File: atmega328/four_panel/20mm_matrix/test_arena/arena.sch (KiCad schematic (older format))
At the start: 35 parts, among them P1 CONN15, P10 CONN_2X2, P11 CONN_2X2, P12 CONN_2X2, P13 CONN_2X2, P14 CONN_2X2, P15 CONN_2X2, P16 CONN_2X2, P17 CONN_2X2, P18 CONN_2X2, P19 CONN_2X2, P2 CONN15, P20 CONN_2X2, P21 CONN_2X2, P22 CONN_20X2, P23 CONN_30X2, P24 CONN_2, P3 CONN15, P4 CONN15, P5 CONN15, P6 CONN15, P7 CONN_2X2, P8 CONN_2X2, P9 CONN_2X2

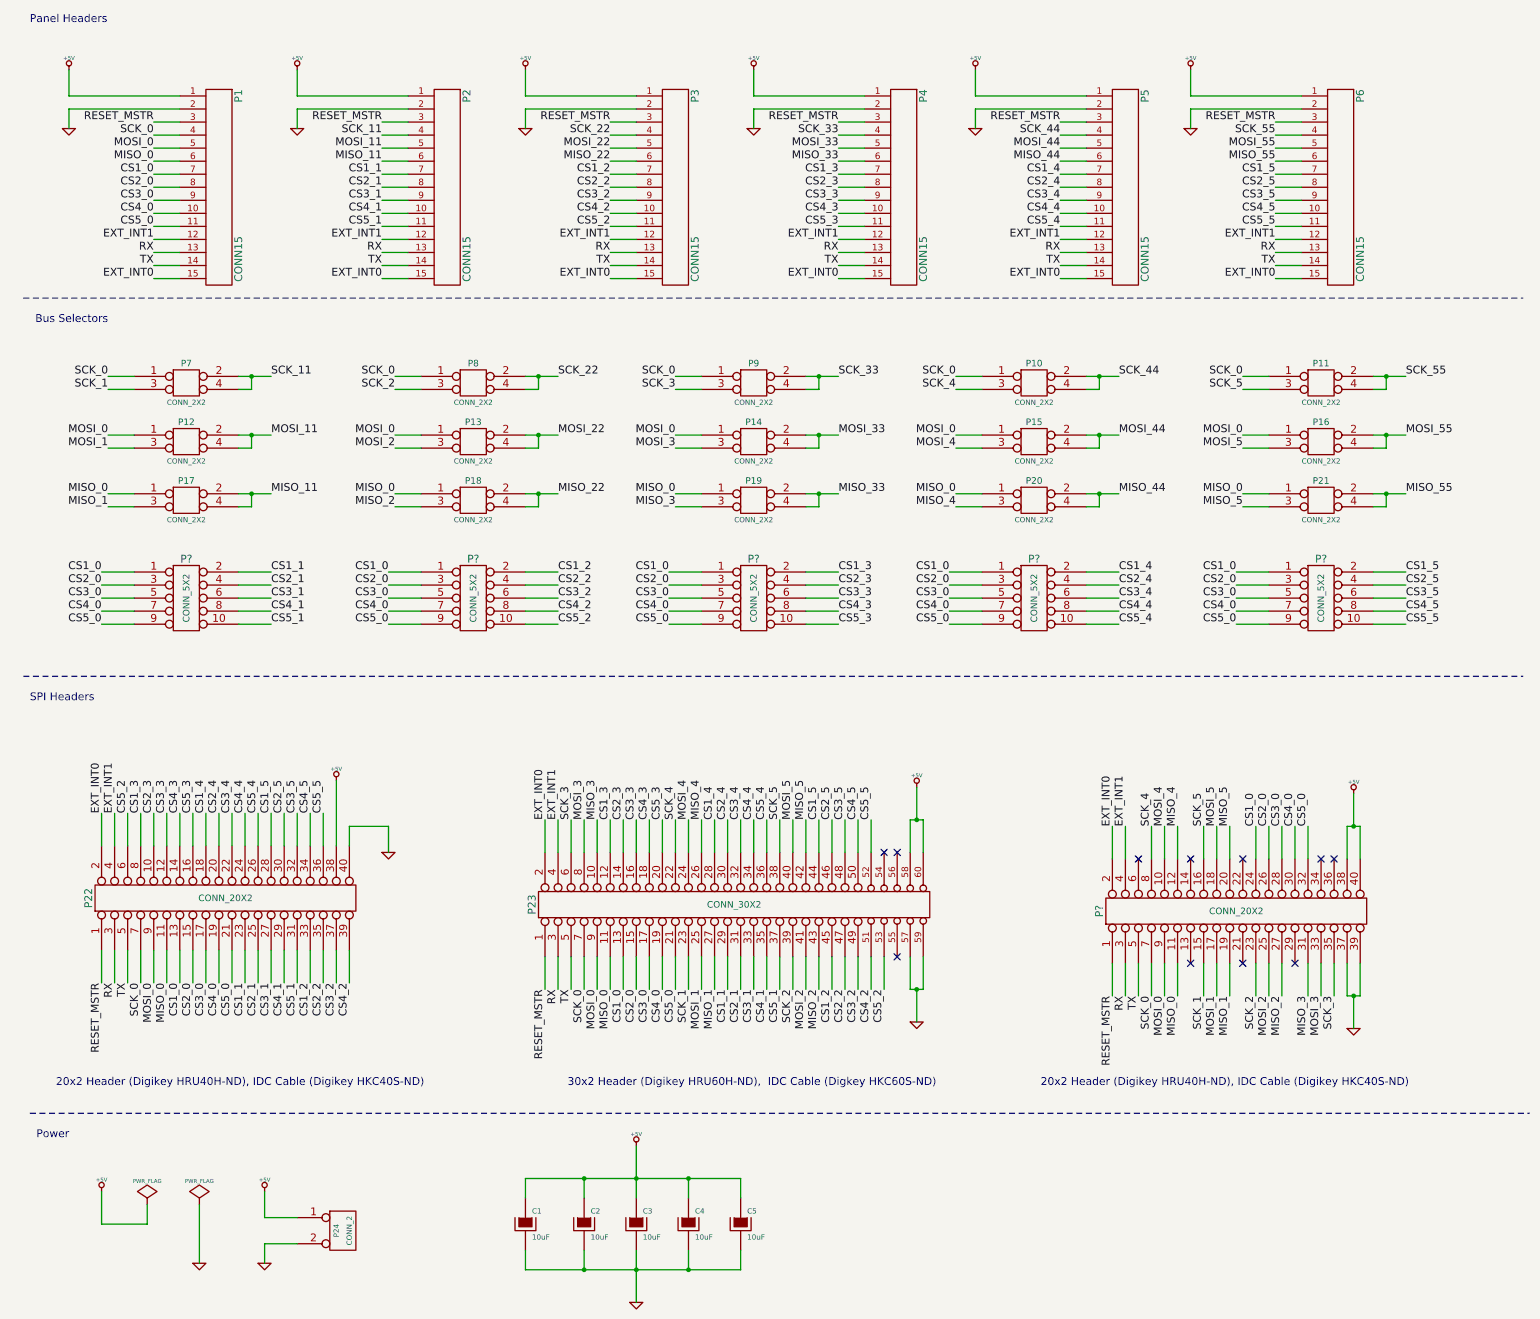
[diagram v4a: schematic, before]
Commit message: Added 3rd spi header to test arenas. Third header has 6 spi buses w/ 5 common cs lines.
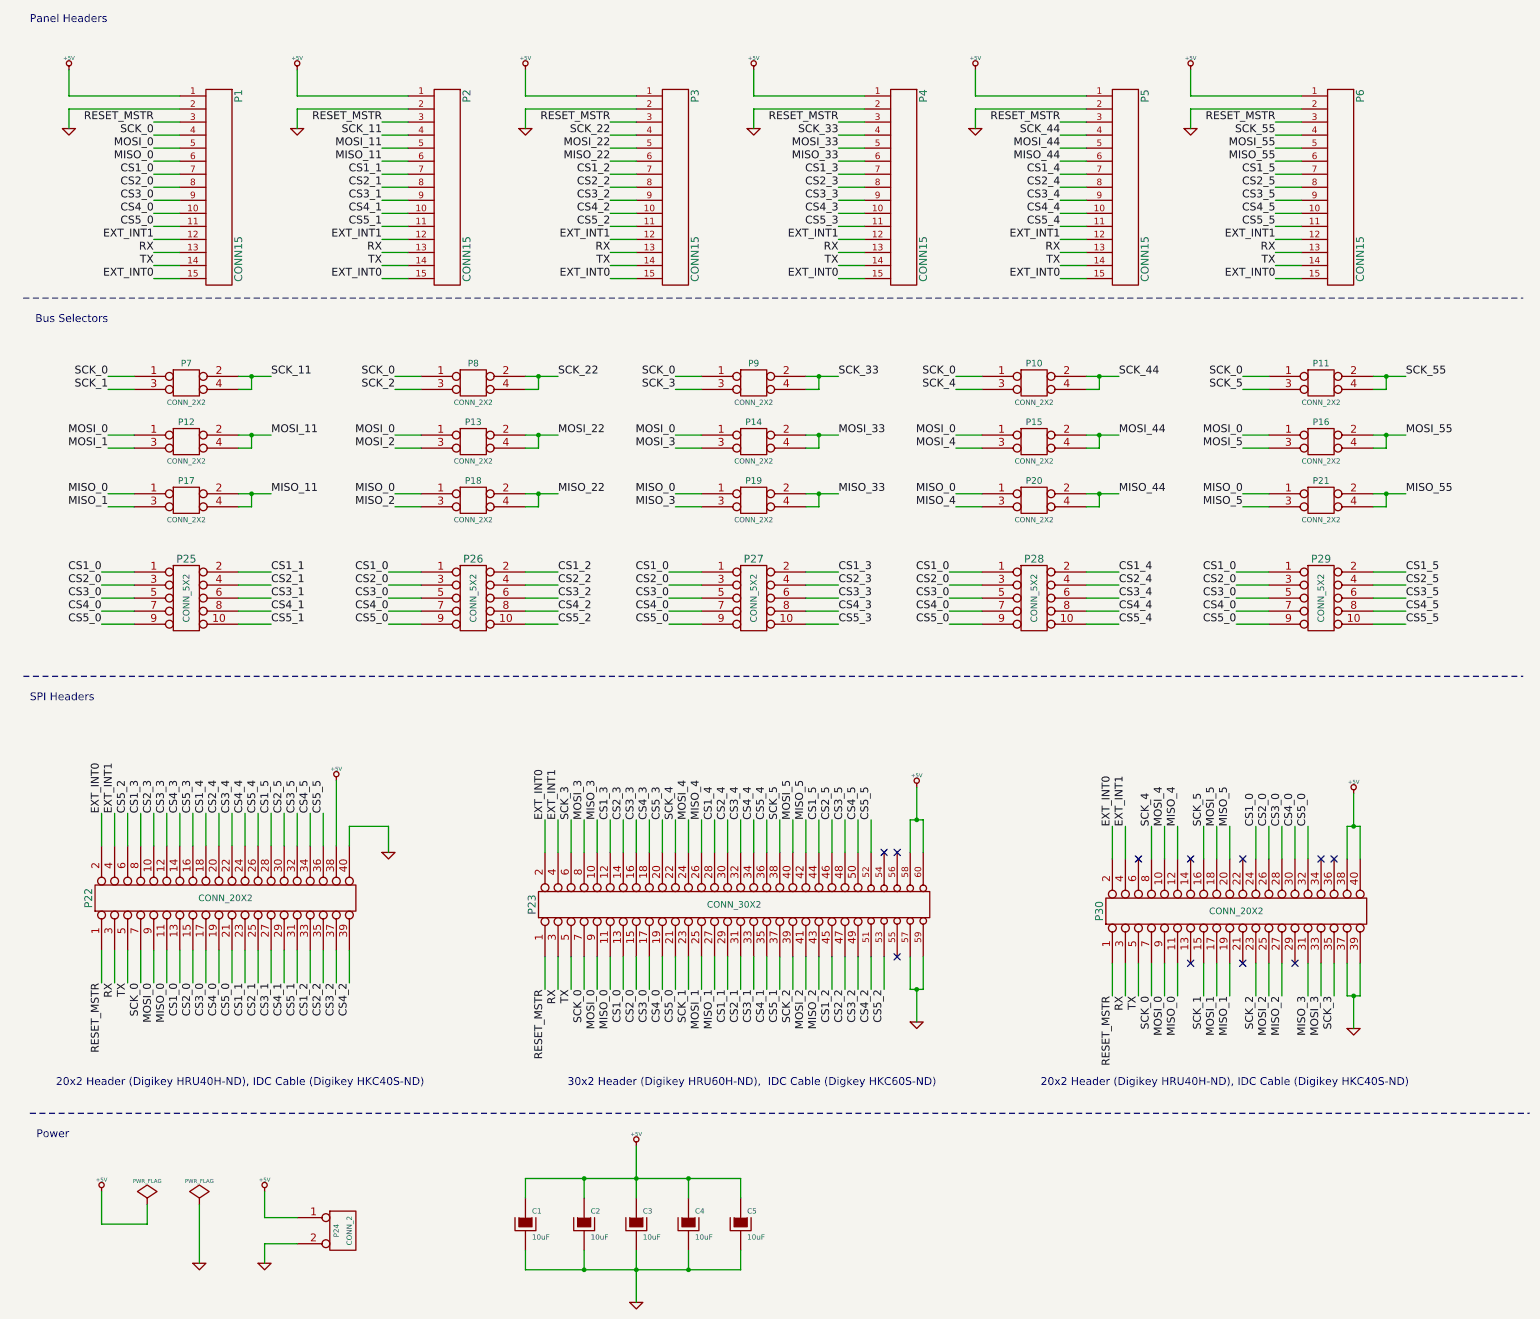
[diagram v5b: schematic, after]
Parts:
- gave numbers to parts that had none: 6
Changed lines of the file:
@@
 NoConn ~ 7200 7800
 Wire Wire Line
-	7300 6750 7350 6750
-Wire Wire Line
-	7350 6750 7400 6750
+	7300 6750 7400 6750
 Wire Wire Line
 	7350 6750 7350 6500
 Connection ~ 7350 6750
 Wire Wire Line
-	7300 8050 7350 8050
-Wire Wire Line
-	7350 8050 7400 8050
+	7300 8050 7400 8050
 Wire Wire Line
 	7350 8050 7350 8300
@@
 	1350 3450 1150 3450
 Wire Wire Line
-	2150 3350 2250 3350
-Wire Wire Line
-	2250 3350 2400 3350
+	2150 3350 2400 3350
 Wire Wire Line
 	2250 3350 2250 3450
@@
 	2250 3900 2250 3800
 Wire Wire Line
-	2150 3800 2250 3800
-Wire Wire Line
-	2250 3800 2400 3800
+	2150 3800 2400 3800
 Connection ~ 2250 3800
 Text Label 2400 3800 0    60   ~ 0
@@
 	1350 4350 1150 4350
 Wire Wire Line
-	2150 4250 2250 4250
-Wire Wire Line
-	2250 4250 2400 4250
+	2150 4250 2400 4250
 Wire Wire Line
 	2250 4250 2250 4350
@@
 MISO_2
 Wire Wire Line
-	4350 3350 4450 3350
-Wire Wire Line
-	4450 3350 4600 3350
+	4350 3350 4600 3350
 Wire Wire Line
 	4450 3350 4450 3450
@@
 	4450 3900 4450 3800
 Wire Wire Line
-	4350 3800 4450 3800
-Wire Wire Line
-	4450 3800 4600 3800
+	4350 3800 4600 3800
 Connection ~ 4450 3800
 Text Label 4600 3800 0    60   ~ 0
 MOSI_22
 Wire Wire Line
-	4350 4250 4450 4250
-Wire Wire Line
-	4450 4250 4600 4250
+	4350 4250 4600 4250
 Wire Wire Line
 	4450 4250 4450 4350
@@
 MISO_3
 Wire Wire Line
-	6500 3350 6600 3350
-Wire Wire Line
-	6600 3350 6750 3350
+	6500 3350 6750 3350
 Wire Wire Line
 	6600 3350 6600 3450
@@
 	6600 3900 6600 3800
 Wire Wire Line
-	6500 3800 6600 3800
-Wire Wire Line
-	6600 3800 6750 3800
+	6500 3800 6750 3800
 Connection ~ 6600 3800
 Text Label 6750 3800 0    60   ~ 0
 MOSI_33
 Wire Wire Line
-	6500 4250 6600 4250
-Wire Wire Line
-	6600 4250 6750 4250
+	6500 4250 6750 4250
 Wire Wire Line
 	6600 4250 6600 4350
@@
 MISO_4
 Wire Wire Line
-	8650 3350 8750 3350
-Wire Wire Line
-	8750 3350 8900 3350
+	8650 3350 8900 3350
 Wire Wire Line
 	8750 3350 8750 3450
@@
 	8750 3900 8750 3800
 Wire Wire Line
-	8650 3800 8750 3800
-Wire Wire Line
-	8750 3800 8900 3800
+	8650 3800 8900 3800
 Connection ~ 8750 3800
 Text Label 8900 3800 0    60   ~ 0
 MOSI_44
 Wire Wire Line
-	8650 4250 8750 4250
-Wire Wire Line
-	8750 4250 8900 4250
+	8650 4250 8900 4250
 Wire Wire Line
 	8750 4250 8750 4350
@@
 MISO_5
 Wire Wire Line
-	10850 3350 10950 3350
-Wire Wire Line
-	10950 3350 11100 3350
+	10850 3350 11100 3350
 Wire Wire Line
 	10950 3350 10950 3450
@@
 	10950 3900 10950 3800
 Wire Wire Line
-	10850 3800 10950 3800
-Wire Wire Line
-	10950 3800 11100 3800
+	10850 3800 11100 3800
 Connection ~ 10950 3800
 Text Label 11100 3800 0    60   ~ 0
 MOSI_55
 Wire Wire Line
-	10850 4250 10950 4250
-Wire Wire Line
-	10950 4250 11100 4250
+	10850 4250 11100 4250
 Wire Wire Line
 	10950 4250 10950 4350
@@
 	4350 9650 4350 9500
 Wire Wire Line
-	4350 9500 4800 9500
-Wire Wire Line
-	4800 9500 5200 9500
-Wire Wire Line
-	5200 9500 5600 9500
-Wire Wire Line
-	5600 9500 6000 9500
+	4350 9500 6000 9500
 Wire Wire Line
 	4800 9500 4800 9650
 Wire Wire Line
-	5200 9250 5200 9500
-Wire Wire Line
-	5200 9500 5200 9650
+	5200 9250 5200 9650
 Connection ~ 4800 9500
 Wire Wire Line
@@
 	4350 10050 4350 10200
 Wire Wire Line
-	4350 10200 4800 10200
-Wire Wire Line
-	4800 10200 5200 10200
-Wire Wire Line
-	5200 10200 5600 10200
-Wire Wire Line
-	5600 10200 6000 10200
+	4350 10200 6000 10200
 Wire Wire Line
 	4800 10200 4800 10050
 Wire Wire Line
-	5200 10050 5200 10200
-Wire Wire Line
-	5200 10200 5200 10450
+	5200 10050 5200 10450
 Connection ~ 4800 10200
 Wire Wire Line
@@
 	550  9000 12050 9000
 $Comp
-L CONN_20X2 P?
+L CONN_20X2 P30
 U 1 1 52745318
 P 9800 7450
-F 0 "P?" H 9800 8500 60  0000 C CNN
+F 0 "P30" H 9800 8500 60  0000 C CNN
 F 1 "CONN_20X2" V 9800 7450 50  0000 C CNN
 F 2 "" H 9800 7450 60  0000 C CNN
@@
 CS5_2
 Wire Wire Line
-	10650 8100 10700 8100
-Wire Wire Line
-	10700 8100 10750 8100
+	10650 8100 10750 8100
 Wire Wire Line
 	10700 8100 10700 8350
 Connection ~ 10700 8100
 $Comp
-L GND #PWR?
+L GND #PWR025
 U 1 1 52745376
 P 10700 8350
-F 0 "#PWR?" H 10700 8350 30  0001 C CNN
+F 0 "#PWR025" H 10700 8350 30  0001 C CNN
 F 1 "GND" H 10700 8280 30  0001 C CNN
 F 2 "" H 10700 8350 60  0000 C CNN
@@
 CS5_0
 Wire Wire Line
-	10650 6800 10700 6800
-Wire Wire Line
-	10700 6800 10750 6800
+	10650 6800 10750 6800
 Wire Wire Line
 	10700 6800 10700 6550
 Connection ~ 10700 6800
 $Comp
-L +5V #PWR?
+L +5V #PWR026
 U 1 1 527453C2
 P 10700 6550
-F 0 "#PWR?" H 10700 6640 20  0001 C CNN
+F 0 "#PWR026" H 10700 6640 20  0001 C CNN
 F 1 "+5V" H 10700 6640 30  0000 C CNN
 F 2 "" H 10700 6550 60  0000 C CNN
@@
 CS5_0
 $Comp
-L CONN_5X2 P?
+L CONN_5X2 P25
 U 1 1 527456CD
 P 1750 5050
-F 0 "P?" H 1750 5350 60  0000 C CNN
+F 0 "P25" H 1750 5350 60  0000 C CNN
 F 1 "CONN_5X2" V 1750 5050 50  0000 C CNN
 F 2 "" H 1750 5050 60  0000 C CNN
@@
 $EndComp
 $Comp
-L CONN_5X2 P?
+L CONN_5X2 P26
 U 1 1 527456DC
 P 3950 5050
-F 0 "P?" H 3950 5350 60  0000 C CNN
+F 0 "P26" H 3950 5350 60  0000 C CNN
 F 1 "CONN_5X2" V 3950 5050 50  0000 C CNN
 F 2 "" H 3950 5050 60  0000 C CNN
@@
 $EndComp
 $Comp
-L CONN_5X2 P?
+L CONN_5X2 P27
 U 1 1 527456EB
 P 6100 5050
-F 0 "P?" H 6100 5350 60  0000 C CNN
+F 0 "P27" H 6100 5350 60  0000 C CNN
 F 1 "CONN_5X2" V 6100 5050 50  0000 C CNN
 F 2 "" H 6100 5050 60  0000 C CNN
@@
 $EndComp
 $Comp
-L CONN_5X2 P?
+L CONN_5X2 P28
 U 1 1 527456FA
 P 8250 5050
-F 0 "P?" H 8250 5350 60  0000 C CNN
+F 0 "P28" H 8250 5350 60  0000 C CNN
 F 1 "CONN_5X2" V 8250 5050 50  0000 C CNN
 F 2 "" H 8250 5050 60  0000 C CNN
@@
 $EndComp
 $Comp
-L CONN_5X2 P?
+L CONN_5X2 P29
 U 1 1 52745709
 P 10450 5050
-F 0 "P?" H 10450 5350 60  0000 C CNN
+F 0 "P29" H 10450 5350 60  0000 C CNN
 F 1 "CONN_5X2" V 10450 5050 50  0000 C CNN
 F 2 "" H 10450 5050 60  0000 C CNN
